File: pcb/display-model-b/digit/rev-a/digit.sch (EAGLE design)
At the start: 51 parts, among them J1 DL-100-HEADER-02-EDGE, J10 SOLDER_JUMPER_3, J11 SOLDER_JUMPER_3, J2 DL-100-HEADER-02-EDGE, Q1 MMBT3904, Q2 MMBT3904, Q3 MMBT3904, Q4 MMBT3904, Q5 MMBT3904, Q6 MMBT3904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

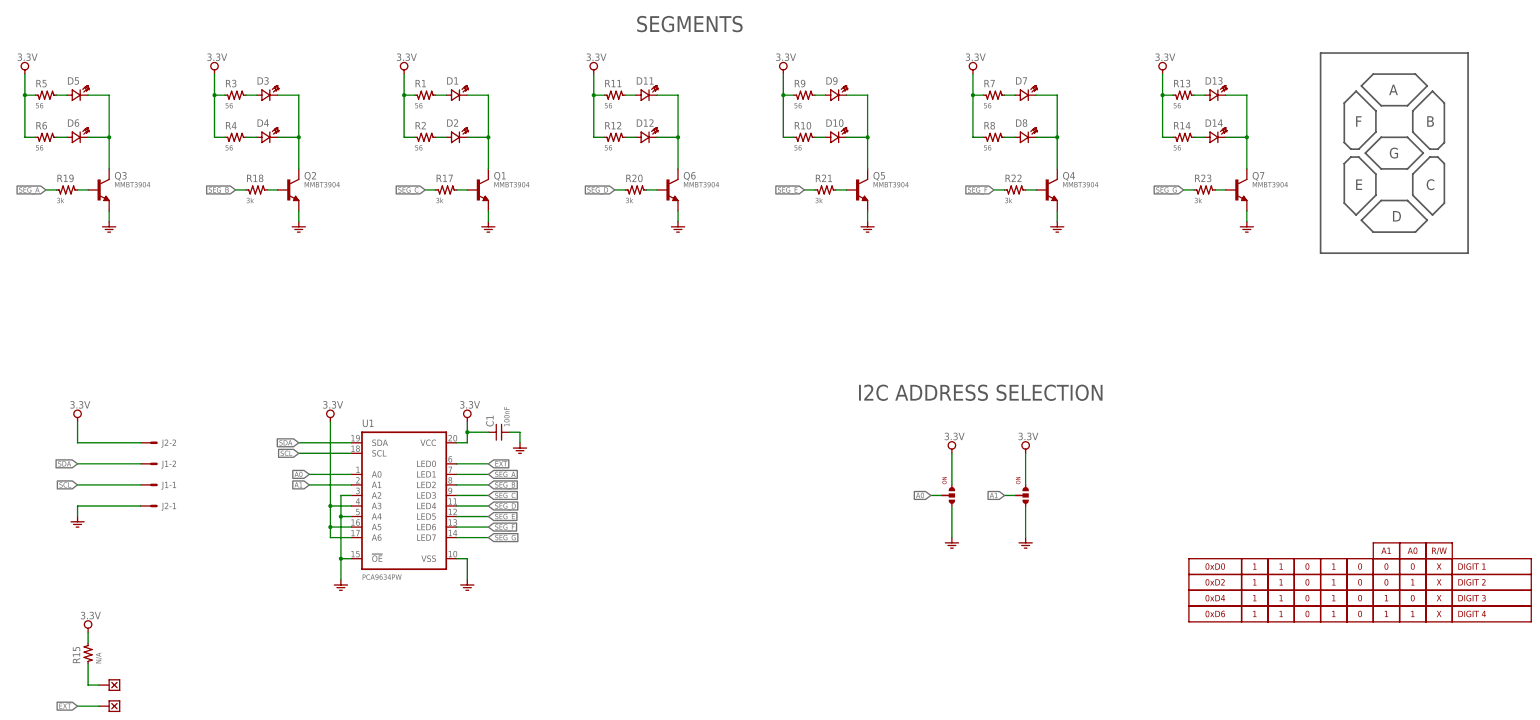
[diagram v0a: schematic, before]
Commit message: Corrected drawings of touch panel PCB
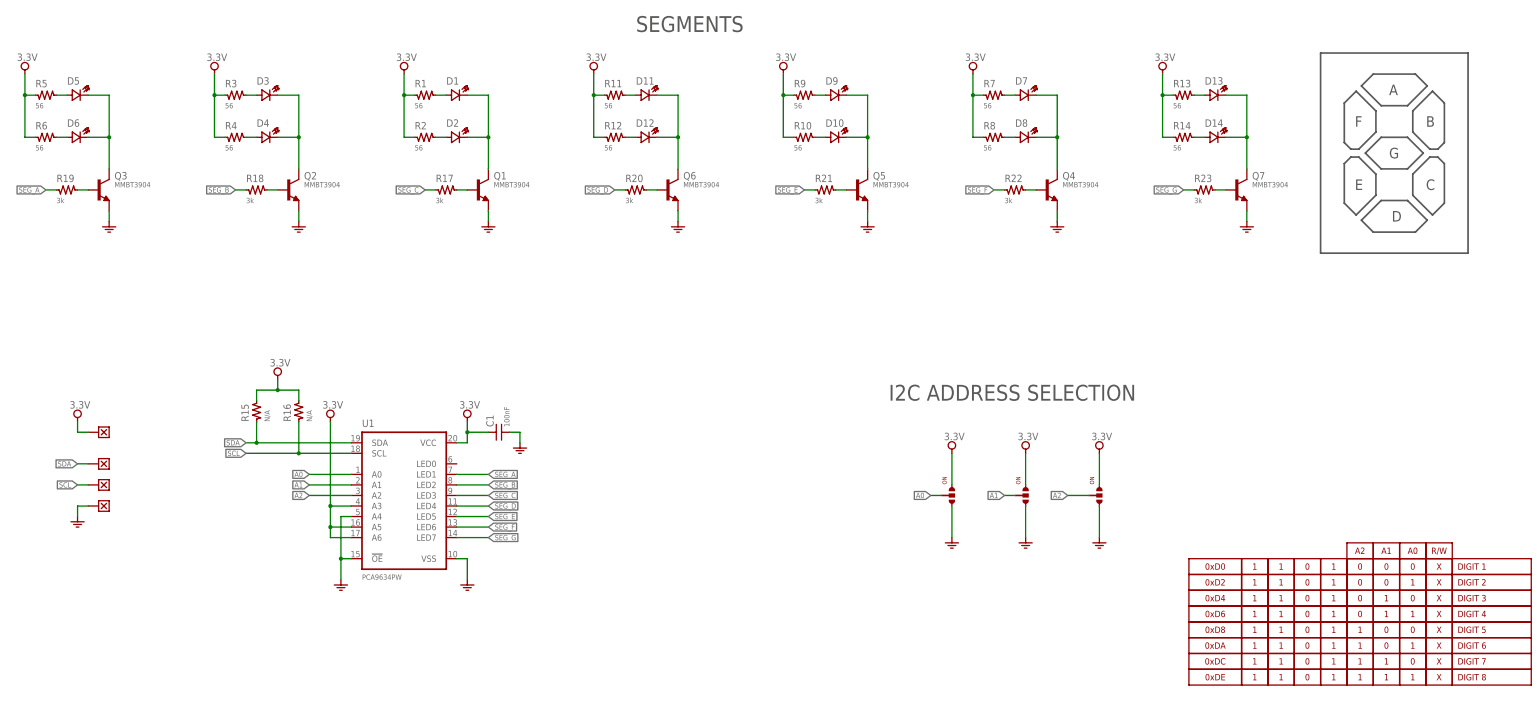
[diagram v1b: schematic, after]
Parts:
- removed J10, J11: SOLDER_JUMPER_3, Misc:SOLDER_JUMPER_3
- removed W5, W6: (no value), Misc:WIRE
- added J3: SOLDER_JUMPER_3, Misc:SOLDER_JUMPER_3
- added R16: N/A, Passive:RES-0603
- added W1, W2, W3, W4: (no value), Misc:WIRE
- D1, D10, D11, D12, D13, D14, D2, D3, D4, D5, D6, D7, D8, D9: PART_NO APT2012SECK/J3-PRV -> (none); SKU (none) -> APT2012SECK/J3-PRV
- J1, J2: value DL-100-HEADER-02-EDGE -> SOLDER_JUMPER_3; device Connectors:DL-100-HEADER-02-EDGE -> Misc:SOLDER_JUMPER_3; MFG Molex -> (none); PART_NO 3-644456-2 -> (none)
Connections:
- removed net EXT: U1.LED0, W5.P$1
- removed net N$30: R15.1, W6.P$1
- new net A2: J3.2, U1.A2
- net 3.3V: now also J1.1, J2.1, J3.1, R16.2, W1.P$1; no longer J10.1, J11.1, J2-2.S
- net A0: now also J2.2; no longer J10.2
- net A1: now also J1.2; no longer J11.2
- net GND: now also J1.3, J2.3, J3.3, W4.P$1; no longer J10.3, J11.3, J2-1.S, U1.A2
- net SCL: now also R16.1, W3.P$1; no longer J1-1.S
- net SDA: now also R15.1, W2.P$1; no longer J1-2.S
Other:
- moved on the sheet: R15
